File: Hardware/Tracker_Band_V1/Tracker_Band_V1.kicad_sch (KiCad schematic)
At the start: 57 parts, among them J1 USB_C_USB20, Q1 SSM6L56FE, SW1 EVP-AVAA1A, SW2 EVP-AVAA1A, U1 ESP32-C3-MINI-1-N4, U2 BNO085, U3 RT8010, U4 MCP73832-2-AC, U5 LM66200, U6 IN-PI15TAT5R5G5B, U7 IN-PI15TAT5R5G5B, U8 IN-PI15TAT5R5G5B, U9 IN-PI15TAT5R5G5B, X1 32.768kHz

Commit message: Initial layout finished
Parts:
- added LG1: ~, 00_tracker_fp:AB_logo, symbol 00_tracker_sym:AB_LOGO
- added TP1, TP2, TP3, TP4, TP5, TP6: 1.5mm, TestPoint:TestPoint_Pad_D1.5mm, symbol Connector:TestPoint
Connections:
- net +3.3V: now also TP1.1
- net +BATT: now also TP5.1
- net BNO_CSn: now also R25.2, U1.23 (GPIO9)
- net BNO_INTn: now also R26.2, U1.22 (GPIO8)
- net BNO_MISO: now also U1.19 (GPIO5,_ADC2_CH0,_FSPIWP,_MTDI)
- net BNO_MOSI: now also U1.18 (GPIO4,_ADC1_CH4,_FSPIHD,_MTMS)
- net BNO_RSTn: now also U1.20 (GPIO6,_FSPICLK,_MTCK)
- net BNO_SCL: now also TP3.1
- net BNO_SCLK: now also U1.21 (GPIO7,_FSPID,_MTDO)
- net BNO_SDA: now also TP2.1
- net BUCK_EN_MCU: now also U1.30 (GPIO20,_U0RXD)
- net CHRG_ST: now also U1.13 (GPIO1,_ADC1_CH1,_XTAL_32K_N)
- net GND: now also TP4.1, TP6.1
- net OR_ST: now also U1.16 (GPIO10,_FSPICS0)
- net RGB_LED: now also R27.2, U1.5 (GPIO2,_ADC1_CH2,_FSPIQ)
- net SW_1: now also U1.31 (GPIO21,_U0TXD)
- net SW_2: now also U1.12 (GPIO0,_ADC1_CH0,_XTAL_32K_P)
- net at SW1.3 (K): now also R17.2, SW1.4 (A)
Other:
- note added: "Battery Conn"
- note added: "IMU Internal I2C Conn"
- note removed: "Imax=500mA"

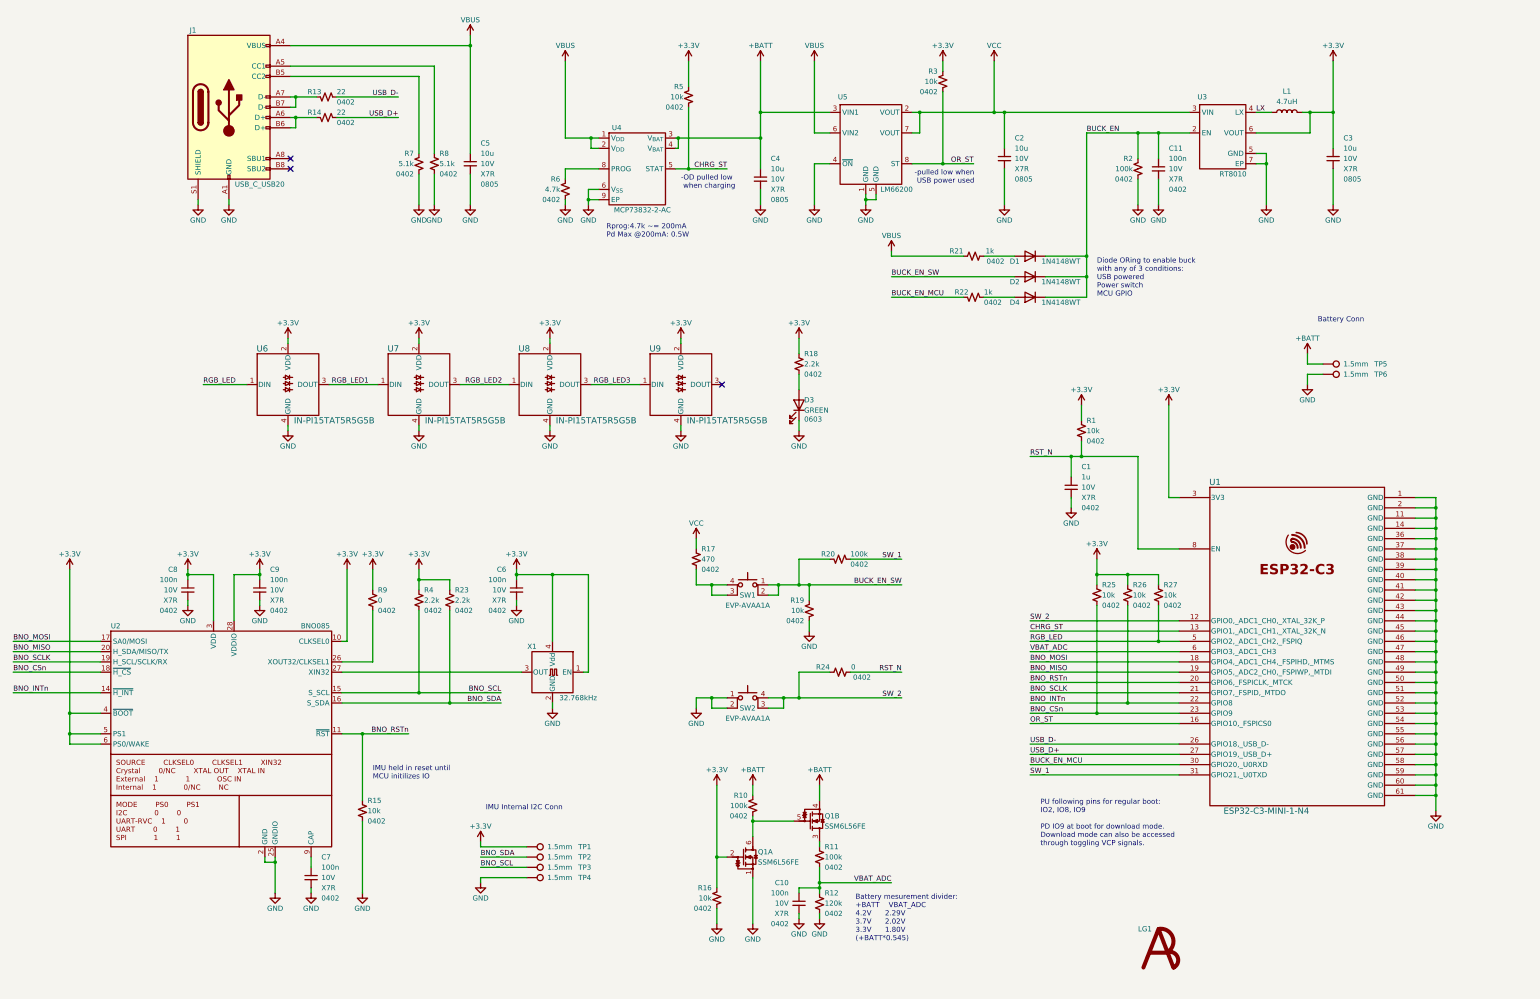
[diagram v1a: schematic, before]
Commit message: DRC Corrected & TPs Added
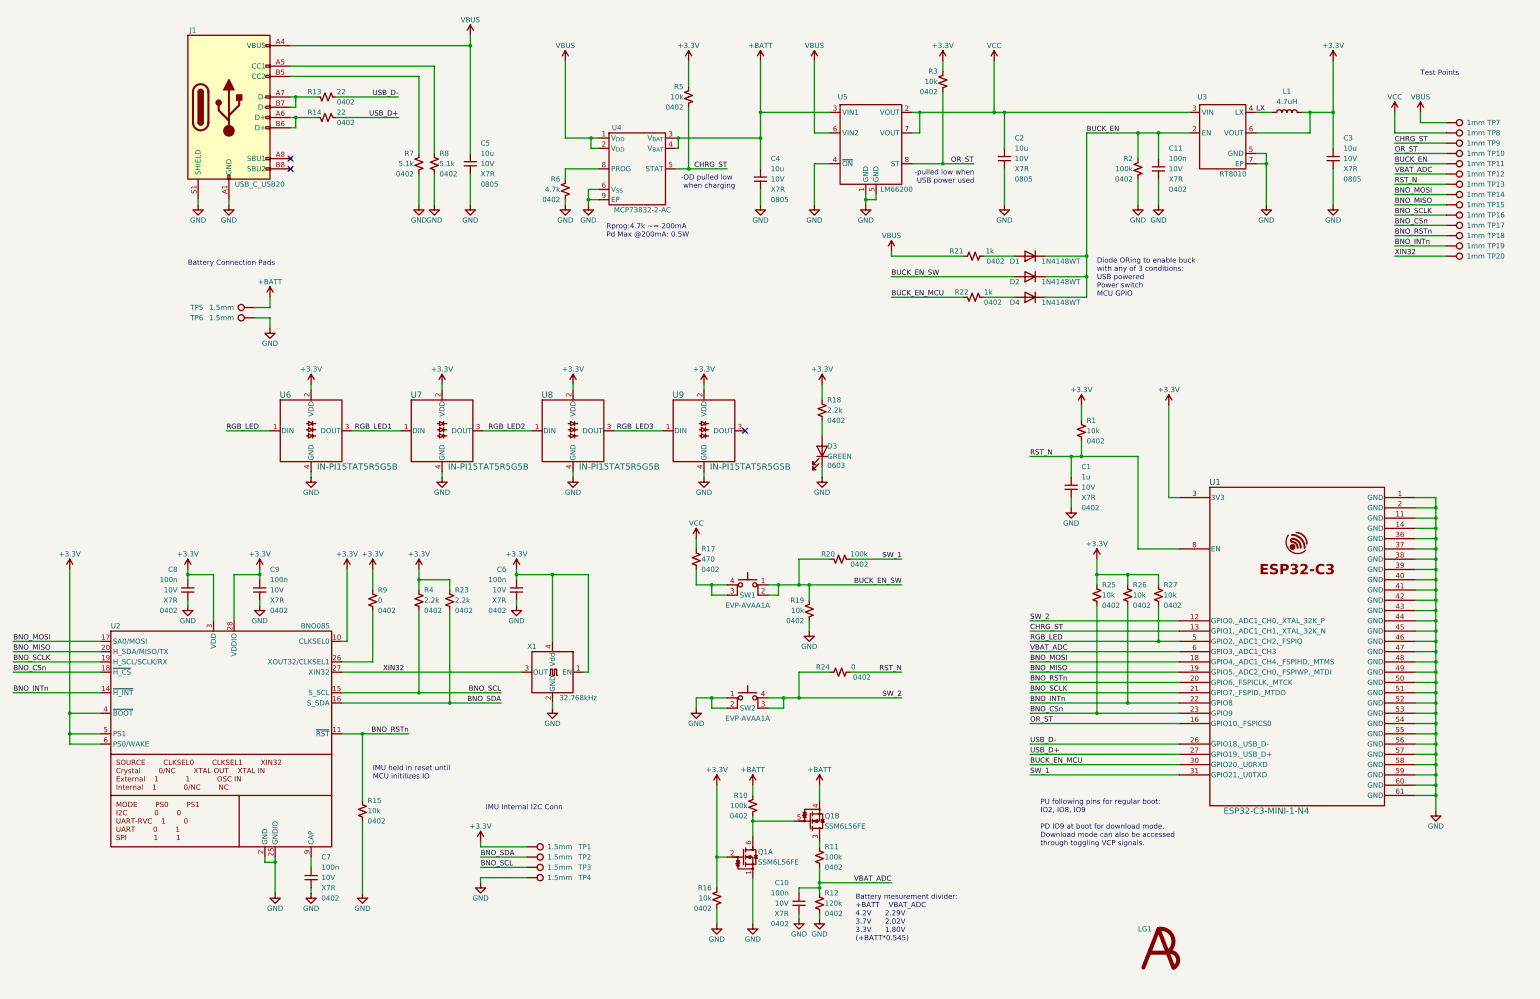
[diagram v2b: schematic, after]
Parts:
- added TP10, TP11, TP12, TP13, TP14, TP15, TP16, TP17, TP18, TP19, TP20, TP7, TP8, TP9: 1mm, TestPoint:TestPoint_Pad_D1.0mm, symbol Connector:TestPoint
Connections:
- net BNO_CSn: now also TP17.1
- net BNO_INTn: now also TP19.1
- net BNO_MISO: now also TP15.1
- net BNO_MOSI: now also TP14.1
- net BNO_RSTn: now also TP18.1
- net BNO_SCLK: now also TP16.1
- net BUCK_EN: now also TP11.1
- net CHRG_ST: now also TP9.1
- net OR_ST: now also TP10.1
- net RST_N: now also TP13.1
- net VBAT_ADC: now also TP12.1
- net VBUS: now also TP7.1
- net VCC: now also TP8.1
- net XIN32: now reaches U2.27 (XIN32), X1.3 (OUT)
- net XIN32: now also TP20.1
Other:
- note added: "Battery Connection Pads"
- note added: "Test Points"
- note removed: "Battery Conn"
- moved on the sheet: D3, R18, TP5, TP6, U6, U7, U8, U9

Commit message: SCH & PCB Finalized for review
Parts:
- R19: value 10k -> 100k
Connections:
- net GND: now also SW2.3 (K), SW2.4 (A); no longer SW2.1, SW2.2
- net SW_2: now also SW2.1, SW2.2; no longer SW2.3 (K), SW2.4 (A)
- now unconnected: U1.10 (NC), U1.15 (NC), U1.17 (NC), U1.24 (NC), U1.25 (NC), U1.28 (NC), U1.29 (NC), U1.32 (NC), U1.33 (NC), U1.34 (NC), U1.35 (NC), U1.4 (NC), U1.7 (NC), U1.9 (NC), U2.1 (PIN1), U2.12 (PIN12), U2.13 (PIN13), U2.21 (PIN21), U2.22 (PIN22), U2.23 (PIN23), U2.24 (PIN24), U2.7 (PIN7), U2.8 (PIN8)
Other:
- note added: "-pulled low when charging"
- note added: "15mA draw at max sample rate, 0.2mA idle"
- note added: "5.1k CC resistors indicate dumb sink device for smart power banks, etc"
- note added: "5mA max per color, 5mA * RGB * 4leds = 60mA total max"
- note added: "Evaluated ~120mA average, 500mA peak"
- note added: "Fixed 3.3V buck, 1A Iout, 100% bypass mode Vin<Vout Expected draw: 120mA + 10mA + 30mA = 160mA Peak draw: 500mA + 15mA + 60mA = 575mA Eff@ 200mA = 96%, Pd = 28mW Eff@ 600mA = 93%, Pd = 150mW Bypass resistance: RdsOn = 0R3, RL = 0R144 Min 3Vout@575mA, 3V + 0.575A * 0R444 = 3.26V min Vin"
- note added: "IMU Internal I2C Connection Pads"
- note added: "Max current draw: 3.3V @ 600mA @ 90% = 450mA @ 4.9V 450mA buck + 200mA charger = 650mA"
- note added: "R24 straps SW2 as user input or reset switch"
- note removed: "-OD pulled low when charging"
- note removed: "IMU Internal I2C Conn"
- company: (none) -> BCIT BENG 2024
- title: (none) -> SilhouetteSync V1
- moved on the sheet: C1, C10, C11, C2, C3, C4, C5, C6, C7, C8, C9, D1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

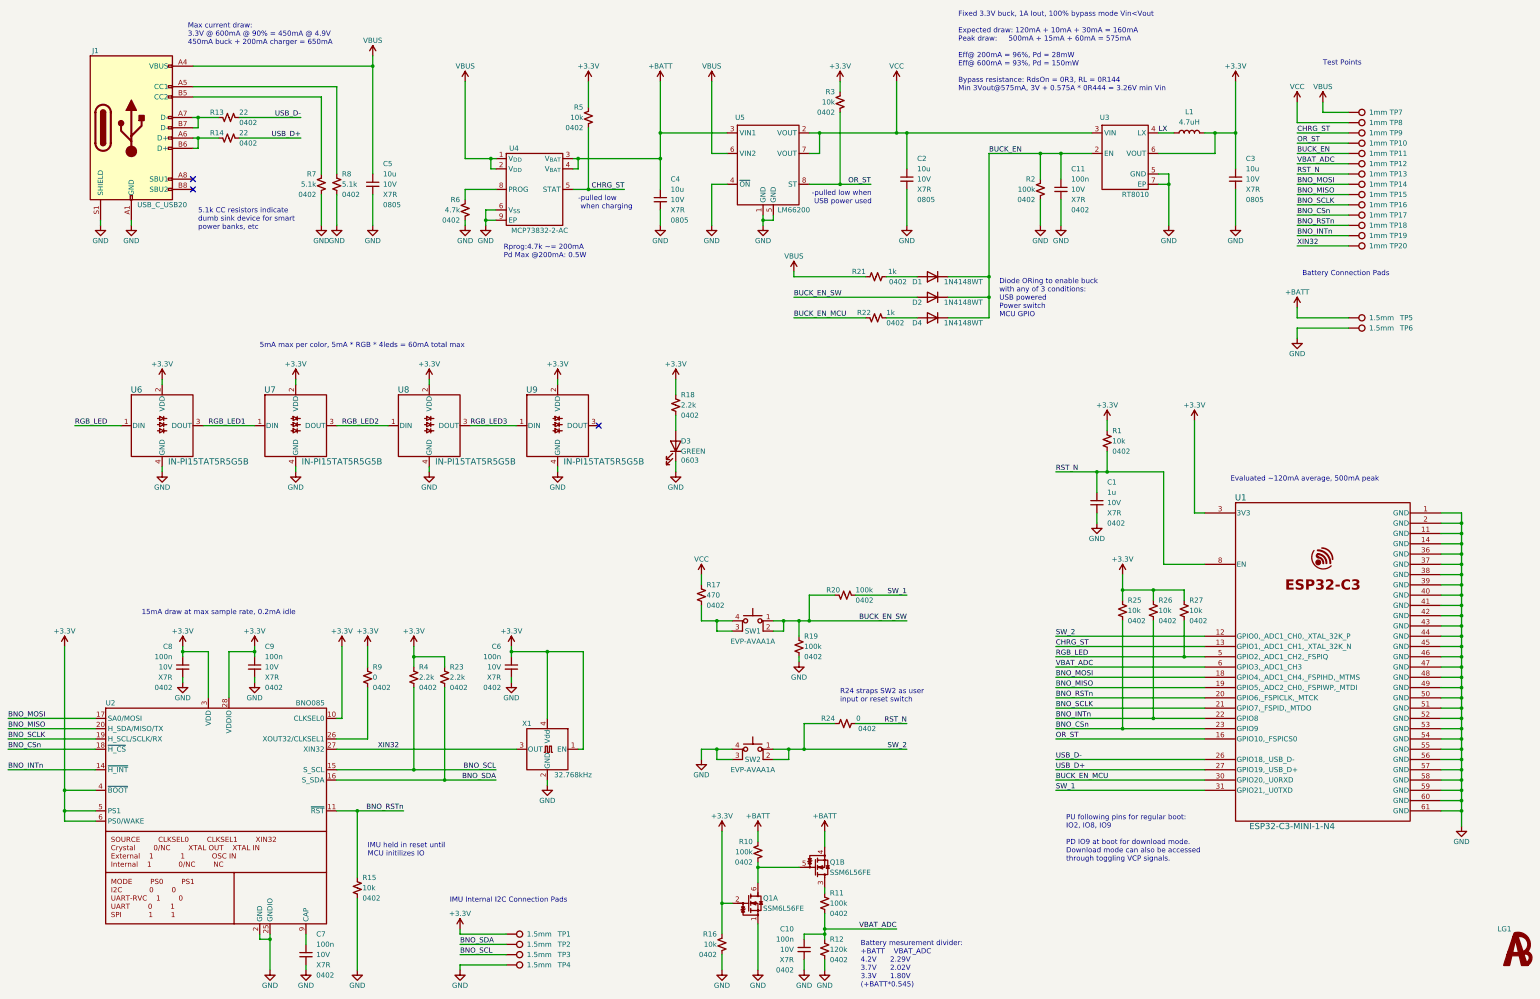
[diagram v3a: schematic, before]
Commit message: Added SBU to USB C
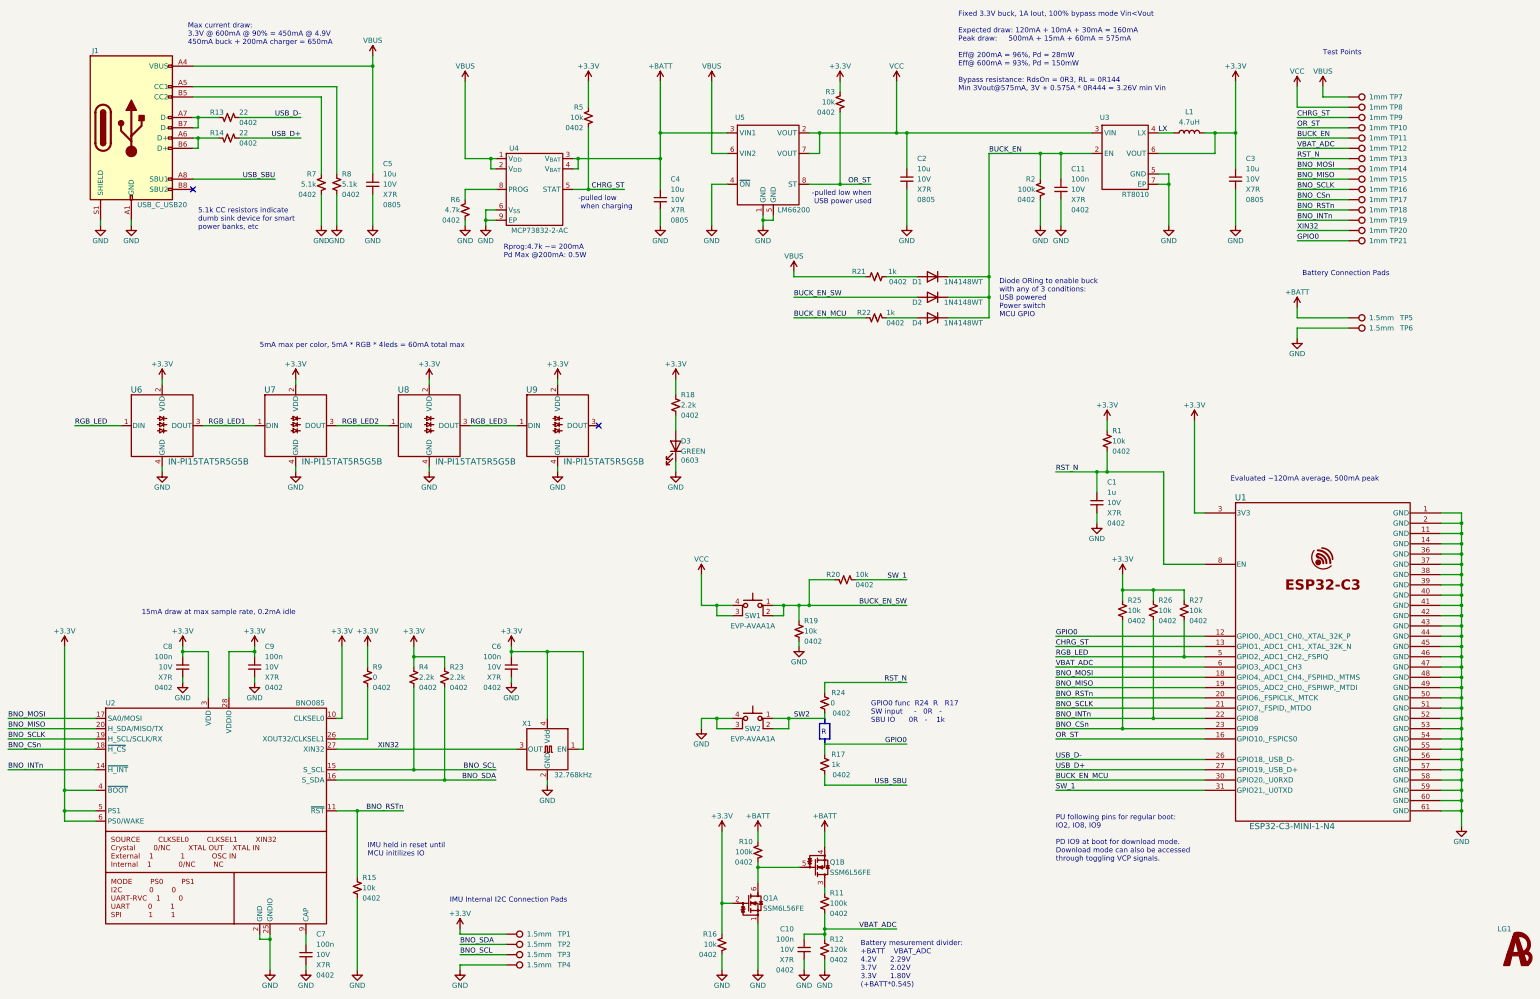
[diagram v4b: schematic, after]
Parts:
- added TP21: 1mm, TestPoint:TestPoint_Pad_D1.0mm, symbol Connector:TestPoint
- R17: value 470 -> 1k
- R19, R20: value 100k -> 10k
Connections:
- net VCC: now also SW1.3 (K), SW1.4 (A); no longer R17.1
- net USB_SBU: now reaches J1.A8 (SBU1)
- net USB_SBU: now also R17.1
- net SW_2 renamed SW2
- net SW2: no longer U1.12 (GPIO0,_ADC1_CH0,_XTAL_32K_P)
- new net GPIO0: R17.2, TP21.1, U1.12 (GPIO0,_ADC1_CH0,_XTAL_32K_P)
- no-connect marks 3 -> 2
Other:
- note added: "GPIO0 func R24 R R17 SW input - 0R - SBU IO 0R - 1k"
- note added: "R"
- note removed: "R24 straps SW2 as user input or reset switch"
- moved on the sheet: R19, R20, R24, SW1, SW2, TP10, TP11, TP12, TP13, TP14, TP15, TP16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

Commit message: Vias updated to plugged 0.3mm & Gerbers Finalized
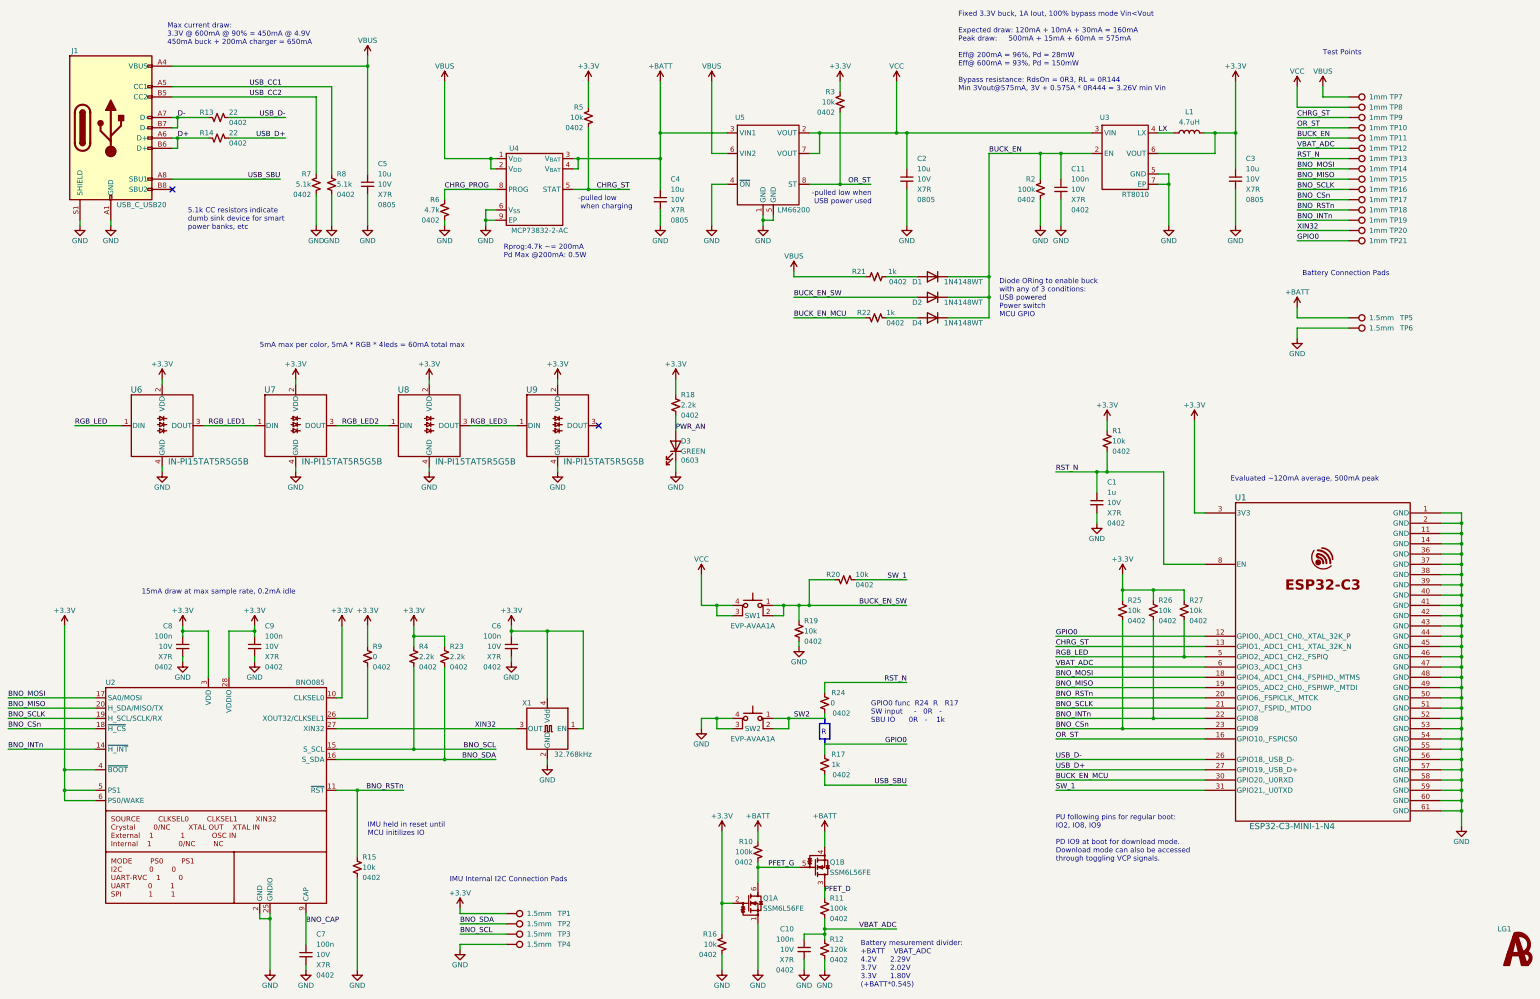
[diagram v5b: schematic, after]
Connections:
- net BNO_CAP: now reaches C7.1, U2.9 (CAP)
- net PFET_D: now reaches Q1.3 (D), R11.1
- net PWR_AN: now reaches D3.2 (A), R18.2
- net USB_CC1: now reaches J1.A5 (CC1), R8.1
- net PFET_G: now reaches Q1.5 (G), Q1.6 (D), R10.2
- net D+: now reaches J1.A6 (D+), J1.B6 (D+), R14.1
- net D-: now reaches J1.A7 (D-), J1.B7 (D-), R13.1
- net USB_CC2: now reaches J1.B5 (CC2), R7.1
- net CHRG_PROG: now reaches R6.1, U4.8 (PROG)
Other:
- moved on the sheet: C5, C6, C8, C9, J1, R11, R13, R14, R15, R23, R4, R6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
